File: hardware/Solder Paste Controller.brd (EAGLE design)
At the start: 120 x 55 mm, 42 parts, among them U1 ATMEGA328P_TQFP, U2 AMS1117, U3 AO3401, U4 ULN2003

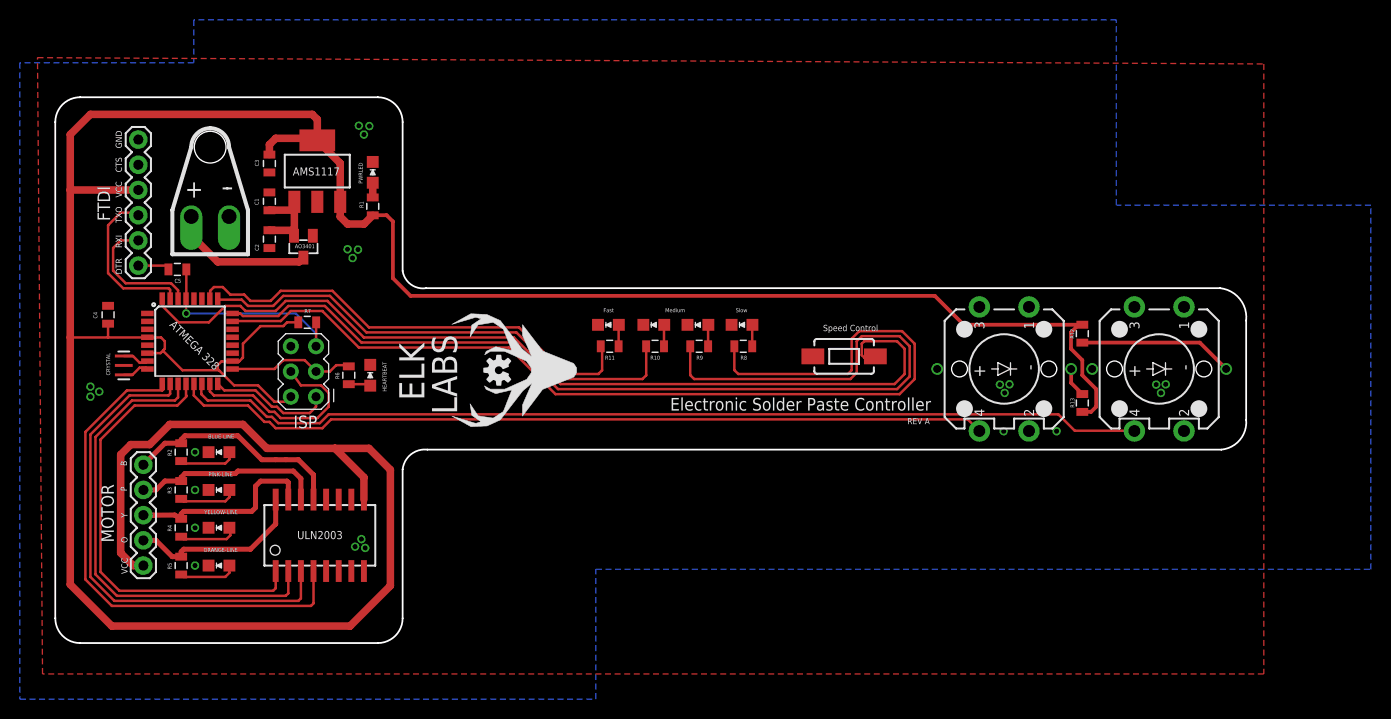
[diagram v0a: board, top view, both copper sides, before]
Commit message: added mounting holes
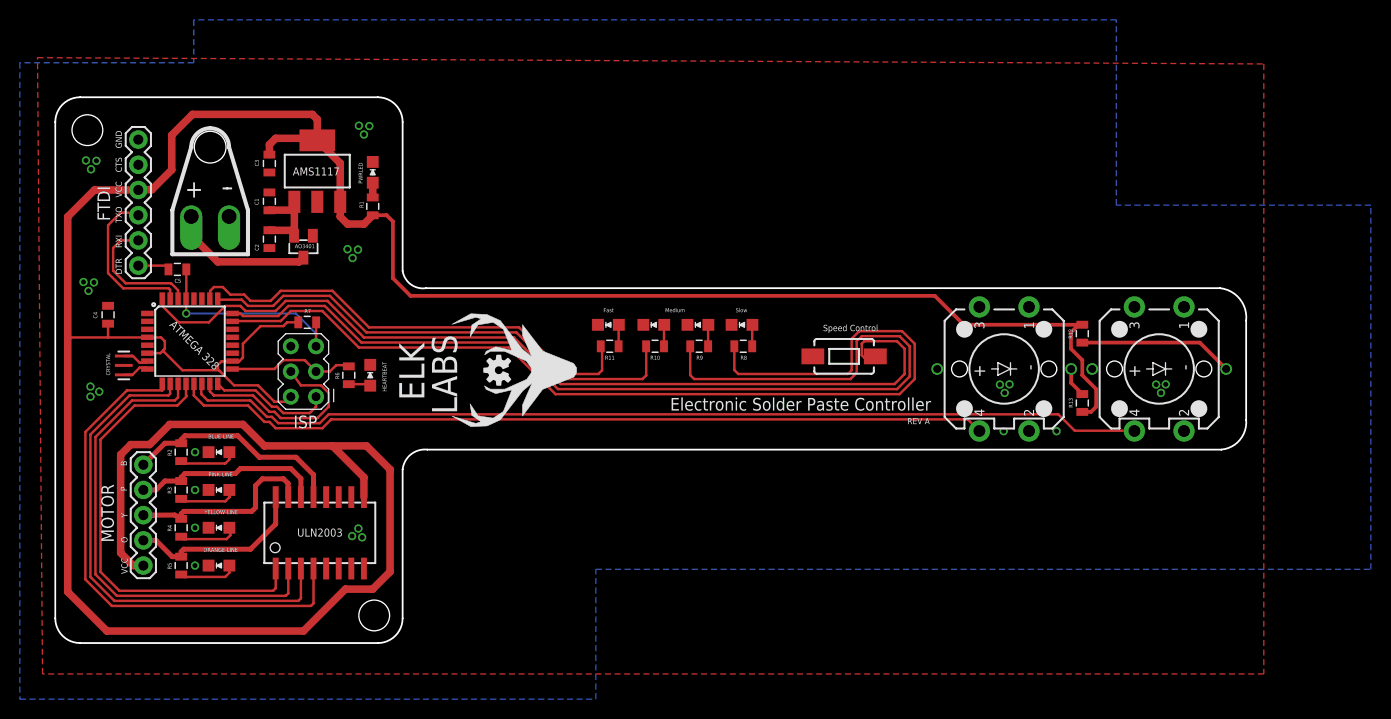
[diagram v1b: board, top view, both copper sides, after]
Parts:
- DC-IN: value POWER-IN-WITH-RELIEF -> red black twister wire
- FTDI: value (none) -> 6 pin header
- MOTOR: value (none) -> 5 pin header
- moved U4 0.25 mm to (26.7, 11.2)
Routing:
- net VCC: track 327.9 -> 319.1 mm
